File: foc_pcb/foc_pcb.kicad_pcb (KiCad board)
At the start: 2 copper layers, 114.3 x 128.3 mm, 70 parts, among them IC1 AS5600-ASOT, J1 Conn_01x03, J10 Conn_02x03_Top_Bottom, J11 Conn_01x03, J12 10118193-0001LF, J2 Conn_01x03, J3 Conn_01x03, J4 Conn_01x04, J5 XT60PW-M, J6 XT60PW-M, J7 Conn_01x02, J8 Conn_01x02, J9 Conn_01x02, SW1 SW_Push, U1 DRV8313PWPR, U2 ATMEGA328P-AU, U3 BSS138-7-F, U4 BSS138-7-F, U5 CH340C, Y1 ABM3-16MHZ

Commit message: V2 redesign done, needs review
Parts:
- removed D2: 1N5819HW-7-F, 1N5819HW-7-F:SOD3715X145N
- removed D3: LED, KT-0603R:LED0603-RD
- removed H10, H11, H12, H9: boardMount, MountingHole:MountingHole_3.2mm_M3
- removed H5, H6, H7, H8: motorMount, MountingHole:MountingHole_3.2mm_M3
- removed J11, J2: Conn_01x03, Connector_PinHeader_2.54mm:PinHeader_1x03_P2.54mm_Vertical
- removed J4: Conn_01x04, Connector_PinHeader_2.54mm:PinHeader_1x04_P2.54mm_Vertical
- removed J7: Conn_01x02, Connector_PinHeader_2.54mm:PinHeader_1x02_P2.54mm_Vertical
- added U6: ~, XIAO-ESP32S3:MOUDLE14P-SMD-2.54-21X17.8MM, F.Cu at (287.7, 126.4)
- added U7: BSS138-7-F, BSS138-7-F:SOT95P240X110-3N, F.Cu at (285.8, 113.0)
- C1, C10, C12, C16, C17, C2, C3, C4, C6, C7, C8, C9, R1, R10, R12, R13, R14, R15, R16, R17, R18, R2, R3, R5, R6, R7: moved to F.Cu
- C11: value VT1V101M-CRE77 -> UWT1V101MCL1GS; footprint VT1V101M-CRE77:CAP-SMD_BD6.3-L6.6-W6.6-FD -> UWT1V101MCL1GS:PCAP_6.3x7.7-ELECT_NCA-L
- C13, C14, IC1, R11, R9: moved to B.Cu
- D1: value 19-213/Y2C-CQ2R2L/3T(CY) -> 1N5819HW-7-F; footprint simpleFOC_led:LED0603-RD-YELLOW -> 1N5819HW-7-F:SOD3715X145N
- D5: footprint KT-0603R:LED0603-RD -> LED_SMD:LED_0603_1608Metric
- J1: value Conn_01x03 -> MPU6050; footprint Connector_PinHeader_2.54mm:PinHeader_1x03_P2.54mm_Vertical -> Connector_PinHeader_2.54mm:PinHeader_1x08_P2.54mm_Vertical
- R4, R8: value 1k -> 10k; moved to F.Cu
- U2: footprint ATMEGA328P-AU-NEW:QFP80P900X900X120-32N -> ATMEGA328P-AU:QFP80P900X900X120-32N
- moved J12 240.4 mm to (229.4, 100.3), turned to 180 degrees
- moved J1 209.3 mm to (284.5, 104.1), turned to -90 degrees
- moved SW1 203.5 mm to (220.2, 120.7), turned to 0 degrees
- moved R5 201.9 mm to (231.6, 118.1), turned to 0 degrees
- moved C9 200.8 mm to (252.7, 114.3), turned to 180 degrees
- moved U5 199.2 mm to (246.4, 114.3)
- moved C12 197.9 mm to (252.0, 109.2), turned to 180 degrees
- moved R13 197.0 mm to (215.1, 105.4), turned to 0 degrees
- moved R6 193.9 mm to (235.4, 118.1)
- moved C10 193.0 mm to (252.0, 111.8), turned to 0 degrees
- moved C4 191.3 mm to (214.6, 118.1), turned to -90 degrees
- moved R7 191.1 mm to (237.5, 118.1)
- moved R14 190.8 mm to (215.1, 109.2), turned to 0 degrees
- moved VR1 190.3 mm to (218.4, 114.3)
- moved R10 187.9 mm to (210.0, 143.5)
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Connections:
- net /escl renamed /scl
- net /esda renamed /sda
- net /lvRX renamed /esp_mosi
- net /lvTX renamed /esp_miso
- C10 pad 1: Net-(U5-V3) -> Net-(U5-VCC)
- C12 pad 2: Net-(U5-V3) -> Net-(U5-VCC)
- J1 pad 1: /uRX -> +3.3V
- J1 pad 2: /uTX -> GND
- J1 pad 3: GND -> /esp_scl_1
- R15 pad 1: /3vin -> +3.3V
- R16 pad 2: /aRX1 -> /mosi
- R17 pad 1: /3vin -> +3.3V
- R18 pad 2: /aTX1 -> /miso
- R4 pad 1: VCC -> +3.3V
- R4 pad 2: Net-(D1-A) -> /esp_sck
- R8 pad 1: Net-(D3-A) -> +5V
- U2 pad 12: /aRX1 -> unconnected-(U2-PB0-Pad12)
- U2 pad 13: /aTX1 -> unconnected-(U2-PB1-Pad13)
- U2 pad 14: /aRX2 -> GND
- U2 pad 23: unconnected-(U2-PC0-Pad23) -> /gpio_1
- U2 pad 24: unconnected-(U2-PC1-Pad24) -> /gpio_2
- U2 pad 32: /aTX2 -> unconnected-(U2-PD2-Pad32)
- U3 pad 1: /3vin -> +3.3V
- U3 pad 3: /aRX1 -> /mosi
- U4 pad 1: /3vin -> +3.3V
- U4 pad 3: /aTX1 -> /miso
- U5 pad 16: +5V -> Net-(U5-VCC)
- U5 pad 4: Net-(U5-V3) -> +5V
- VR1 pad 2: Net-(VR1-OUTPUT) -> +5V
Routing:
- net +5V: track 326.2 -> 76.7 mm, vias 9 -> 13
- net /rst: track 168.6 -> 74.3 mm, vias 2 -> 3
- net /aRX1: track 93.7 -> 0.00 mm, vias 2 -> 0
- net /aTX1: track 88.7 -> 0.00 mm, vias 2 -> 0
- net /uRX: track 92.1 -> 8.32 mm, vias 3 -> 0
- net /uTX: track 83.9 -> 9.68 mm, vias 3 -> 0
- net +3.3V: track 38.4 -> 103.4 mm, vias 1 -> 2
- net /out1: track 67.4 -> 15.3 mm, vias 2 -> 0
- net Net-(U2-PD7): track 75.5 -> 23.9 mm, vias 3 -> 2
- net /in1: track 64.7 -> 16.6 mm, vias 0 -> 2
- net /esp_sda_1: track 0.00 -> 47.9 mm, vias 0 -> 1
- net /out2: track 61.3 -> 15.1 mm, vias 2 -> 0
- net /3vin: track 46.2 -> 0.00 mm
- net /aTX2: track 43.3 -> 0.00 mm
- net VCC: track 35.5 -> 76.0 mm, vias 5 -> 2
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- added copper zone on In1.Cu, net +5V
- added copper zone on In2.Cu, net GND
- removed copper zone on B.Cu, net GND
- removed copper zone on F.Cu, net VCC
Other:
- board size 114.3 x 128.3 mm -> 90.2 x 48.3 mm
- copper layers 2 -> 4

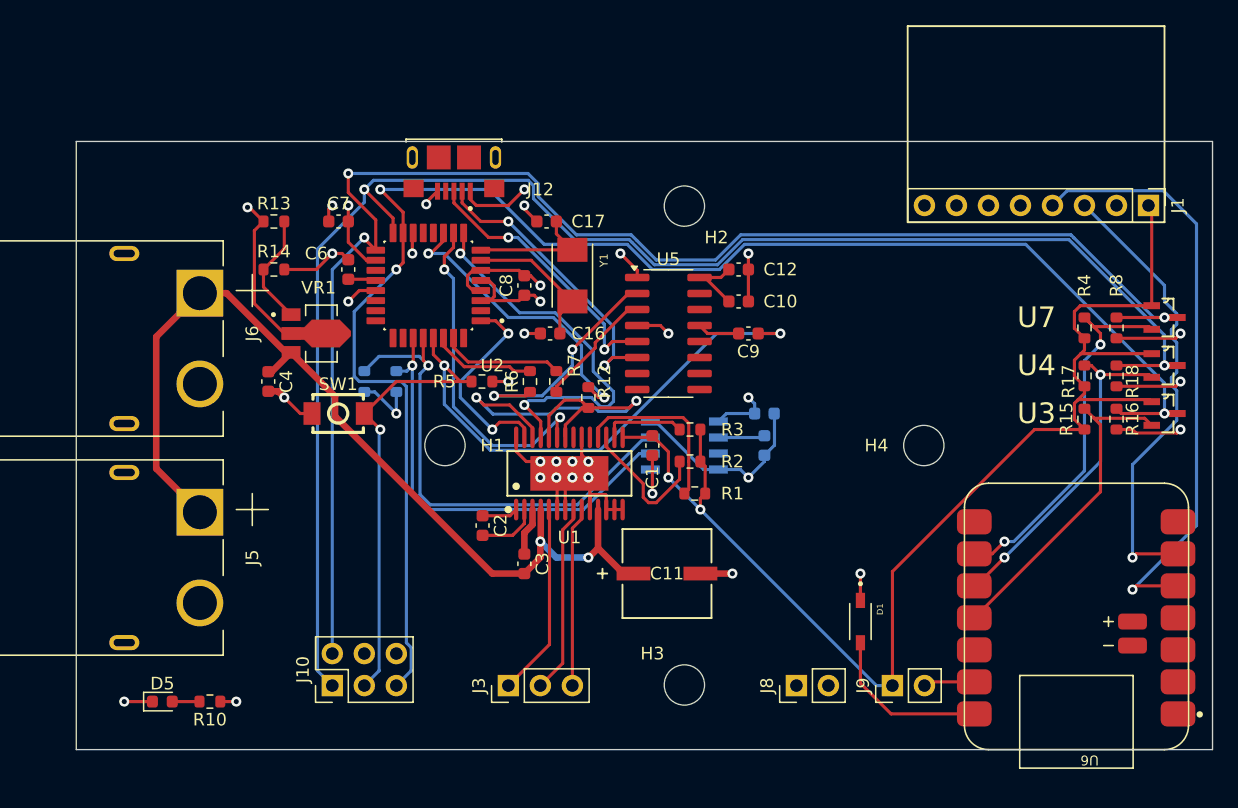
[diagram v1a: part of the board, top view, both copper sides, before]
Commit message: compacted layout, finished V2
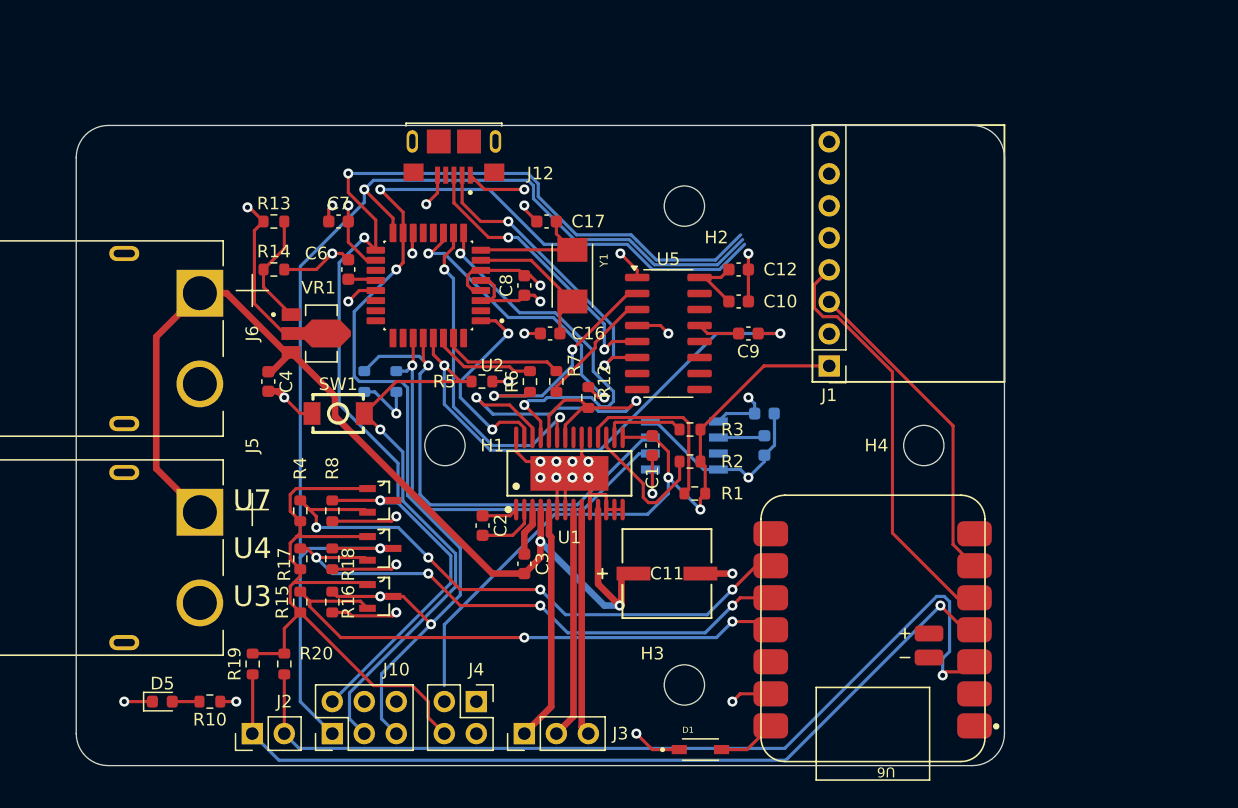
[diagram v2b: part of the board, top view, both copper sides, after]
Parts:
- removed J8, J9: Conn_01x02, Connector_PinHeader_2.54mm:PinHeader_1x02_P2.54mm_Vertical
- added J2: Conn_01x02, Connector_PinHeader_2.54mm:PinHeader_1x02_P2.54mm_Vertical, F.Cu at (213.4, 146.1)
- added J4: power_supply, Connector_PinHeader_2.54mm:PinHeader_2x02_P2.54mm_Vertical, F.Cu at (231.1, 143.5)
- added R19: 10k, Resistor_SMD:R_0603_1608Metric, F.Cu at (213.4, 140.5)
- added R20: 10k, Resistor_SMD:R_0603_1608Metric, F.Cu at (215.9, 140.5)
- moved R15 63.9 mm to (217.2, 135.6)
- moved R16 63.9 mm to (219.7, 135.6)
- moved R17 63.9 mm to (217.2, 132.2)
- moved R18 63.9 mm to (219.7, 132.2)
- moved R4 63.9 mm to (217.2, 128.4)
- moved R8 63.9 mm to (219.7, 128.4)
- moved U3 63.9 mm to (223.5, 135.2)
- moved U4 63.9 mm to (223.5, 131.4)
- moved U7 63.9 mm to (223.5, 127.5)
- moved J1 28.4 mm to (259.1, 116.9), turned to 180 degrees
- moved D1 16.3 mm to (248.9, 147.3), turned to 0 degrees
- moved U6 16.2 mm to (271.5, 127.3)
- moved J3 4.02 mm to (234.9, 146.1)
- moved J10 3.81 mm to (219.7, 146.1)
- moved J12 1.27 mm to (229.4, 99.1)
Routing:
- net /esp_sda_0: track 0.00 -> 72.2 mm, vias 0 -> 1
- net /esp_scl_0: track 0.00 -> 68.8 mm, vias 0 -> 1
- net /mosi: track 124.7 -> 96.3 mm, vias 3 -> 4
- net /miso: track 125.2 -> 97.7 mm
- net /sck: track 120.1 -> 96.3 mm
- net /esp_miso: track 26.7 -> 45.4 mm, vias 2 -> 4
- net /esp_mosi: track 26.1 -> 44.7 mm, vias 0 -> 2
- net /esp_sck: track 30.4 -> 48.9 mm, vias 2 -> 4
- net /esp_sda_1: track 47.9 -> 33.2 mm, vias 1 -> 0
- net /esp_scl_1: track 36.9 -> 25.7 mm, vias 1 -> 0
- net /rst: track 74.3 -> 84.0 mm
- net Net-(U6-5V): track 13.3 -> 4.69 mm
- net VCC: track 76.0 -> 83.3 mm
- net +3.3V: track 103.4 -> 108.3 mm
- net /out3: track 14.3 -> 19.0 mm
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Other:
- board size 90.2 x 48.3 mm -> 73.7 x 50.8 mm

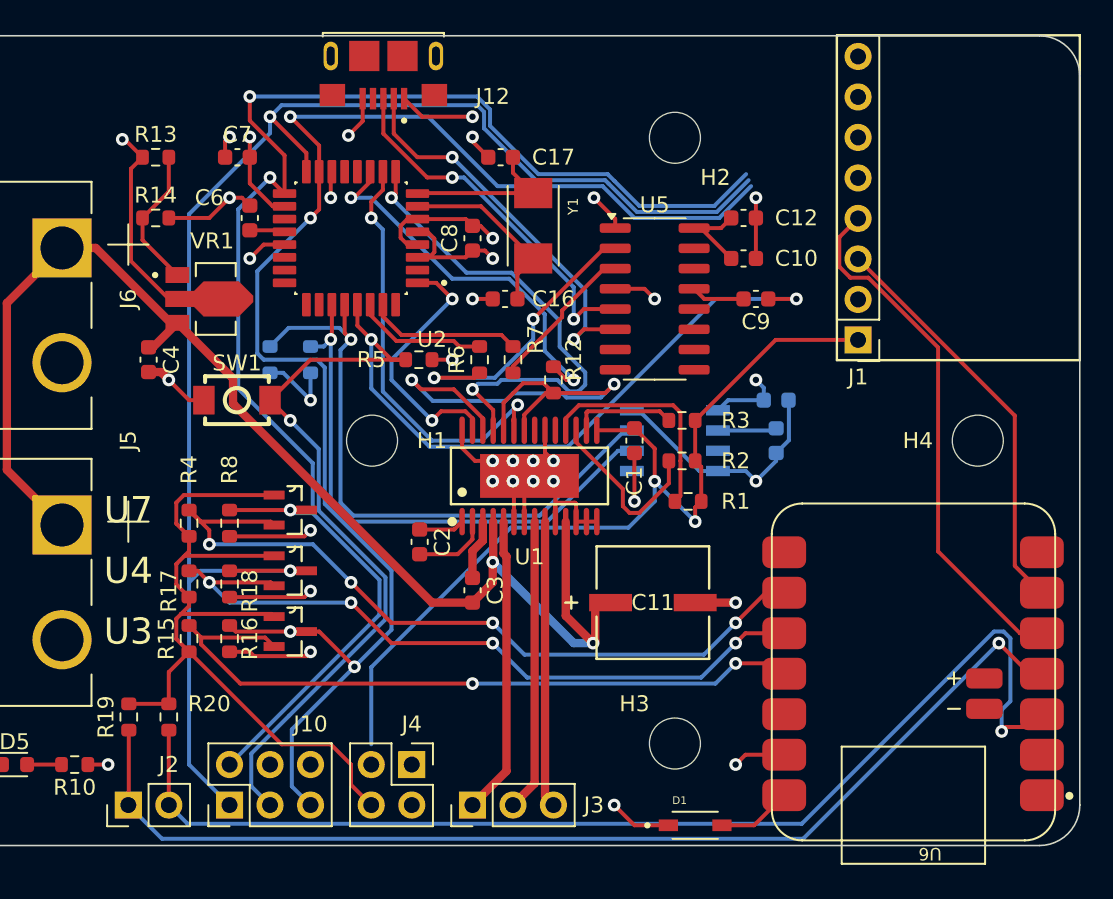
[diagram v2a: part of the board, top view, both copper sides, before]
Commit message: fixed some drc and added silkscreen
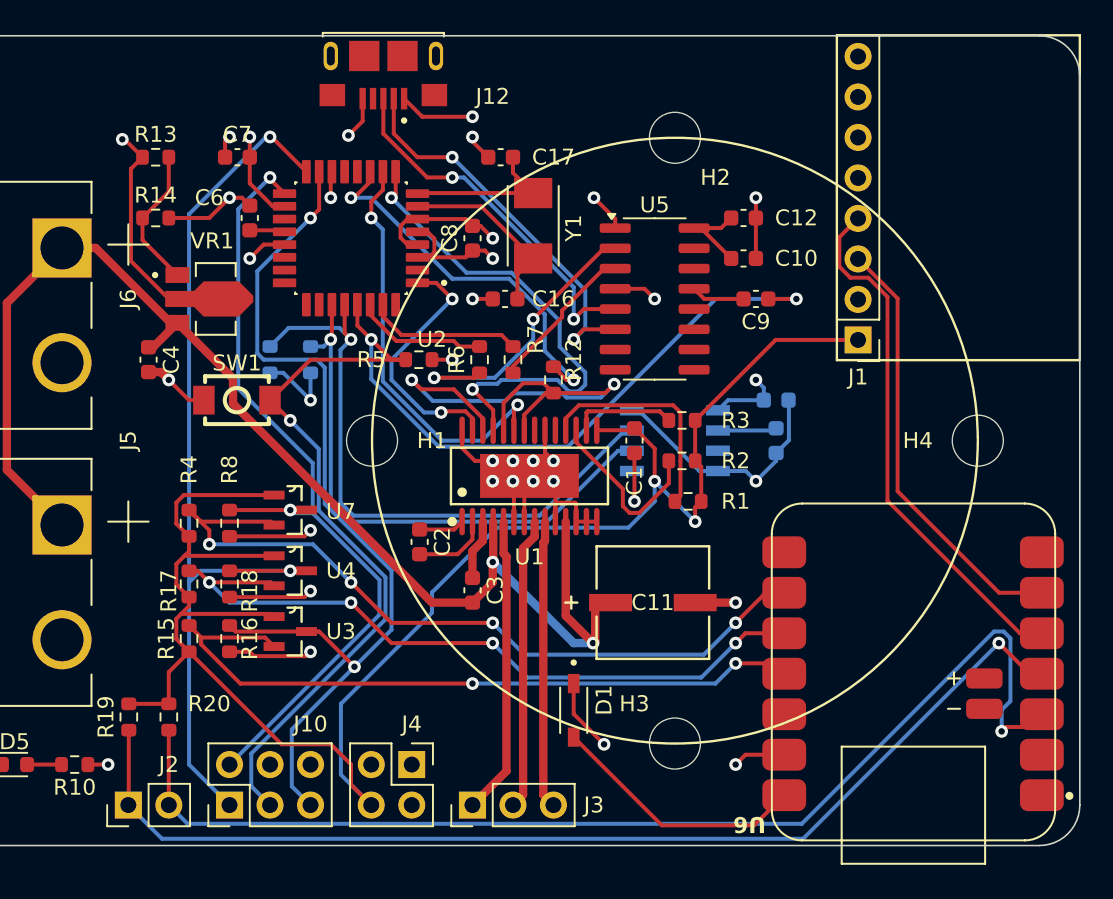
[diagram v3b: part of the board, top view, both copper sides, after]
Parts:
- moved D1 10.5 mm to (241.3, 140.1), turned to -90 degrees
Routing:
- net /sck: track 96.3 -> 53.9 mm, vias 3 -> 2
- net /mosi: track 96.3 -> 58.8 mm, vias 4 -> 2
- net /miso: track 97.7 -> 60.9 mm
- net Net-(U6-5V): track 4.69 -> 16.3 mm
- net +3.3V: track 108.3 -> 114.2 mm
- net /esp_scl_1: track 25.7 -> 27.3 mm
- net +5V: track 77.0 -> 77.7 mm
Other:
- board text added: "AVANINDER.COM"
- board text added: "GimbalFOC"
- board text added: "v2.0"

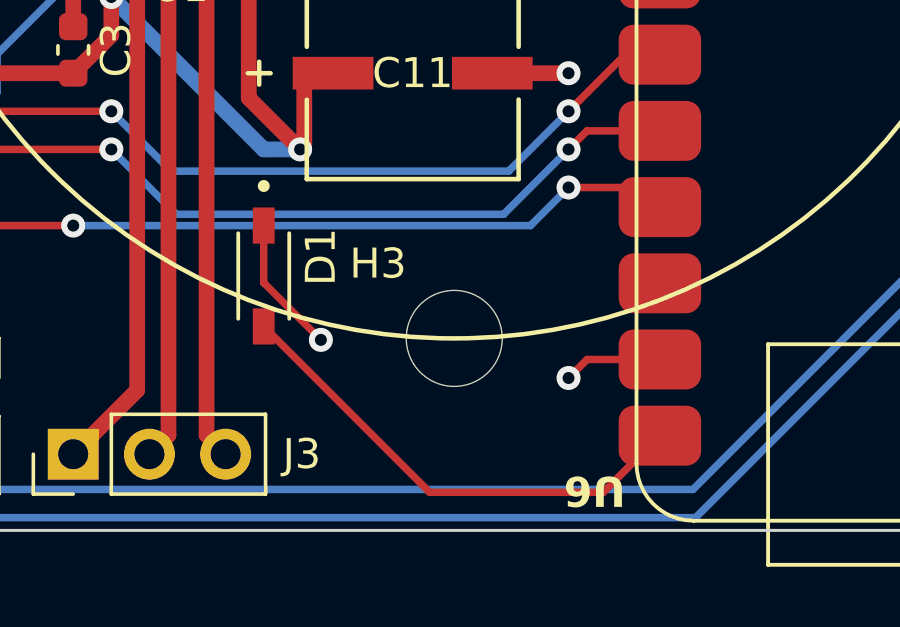
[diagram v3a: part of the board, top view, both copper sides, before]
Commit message: added kicad preview
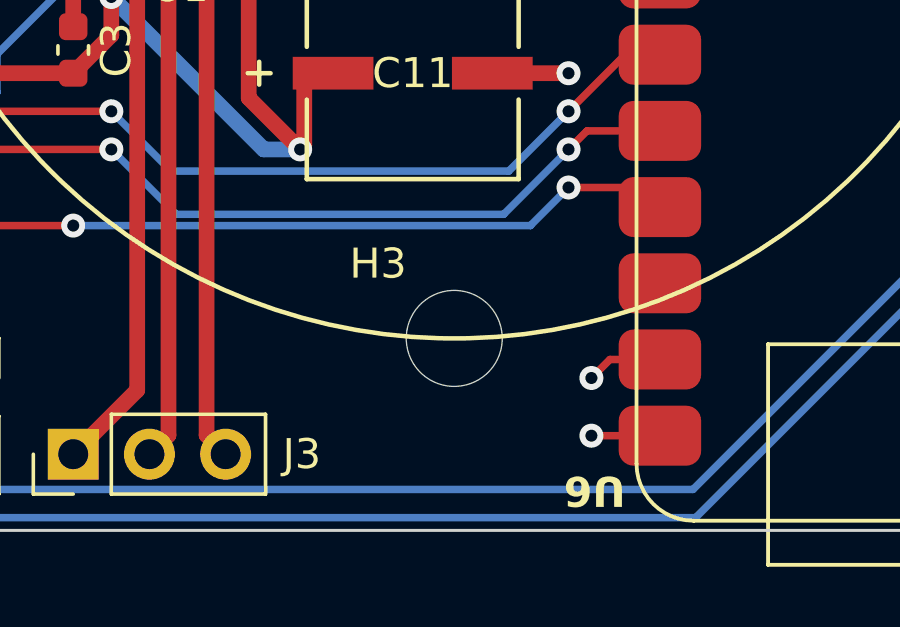
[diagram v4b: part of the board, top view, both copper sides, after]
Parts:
- removed D1: 1N5819HW-7-F, 1N5819HW-7-F:SOD3715X145N
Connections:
- U6 pad 14: Net-(U6-5V) -> +5V
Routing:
- net Net-(U6-5V): track 16.3 -> 0.00 mm
- net +5V: track 77.7 -> 75.4 mm
- net GND: track 81.3 -> 80.5 mm

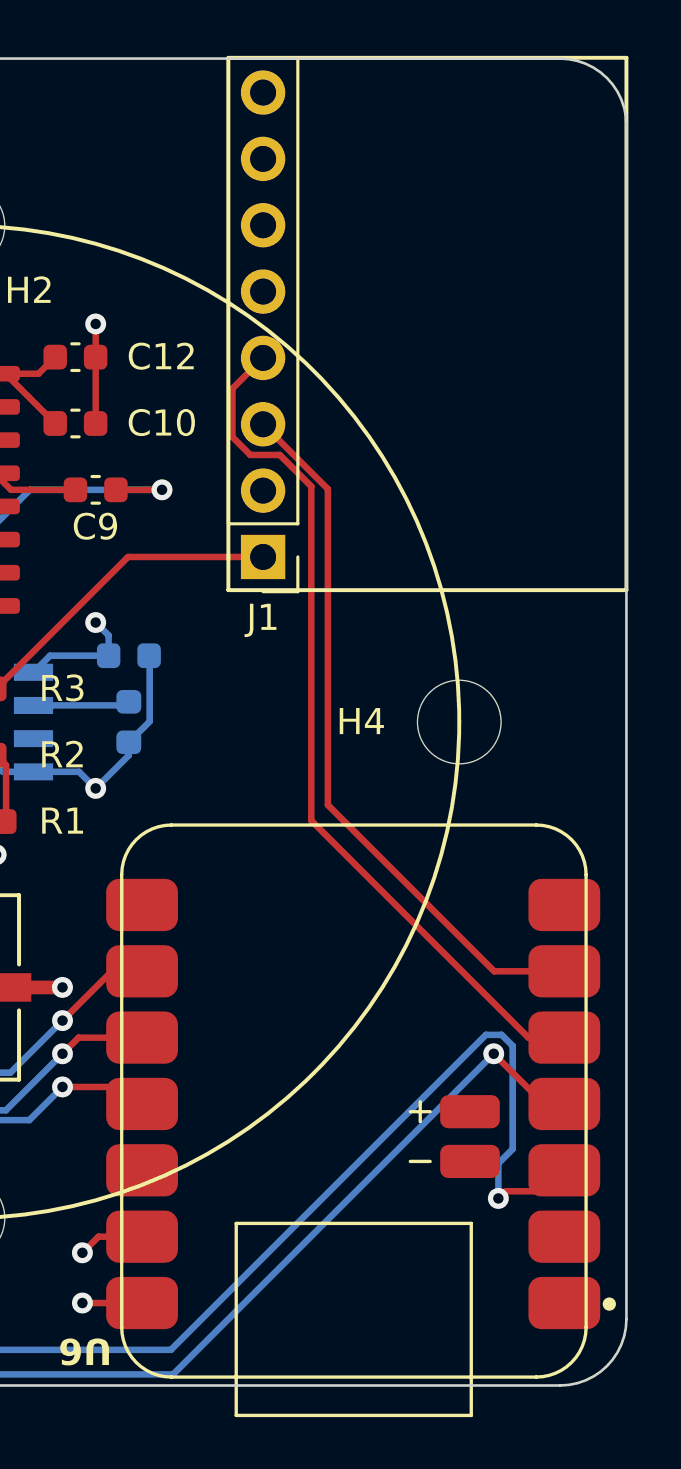
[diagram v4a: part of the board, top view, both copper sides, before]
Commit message: V2 FOC and SPI working
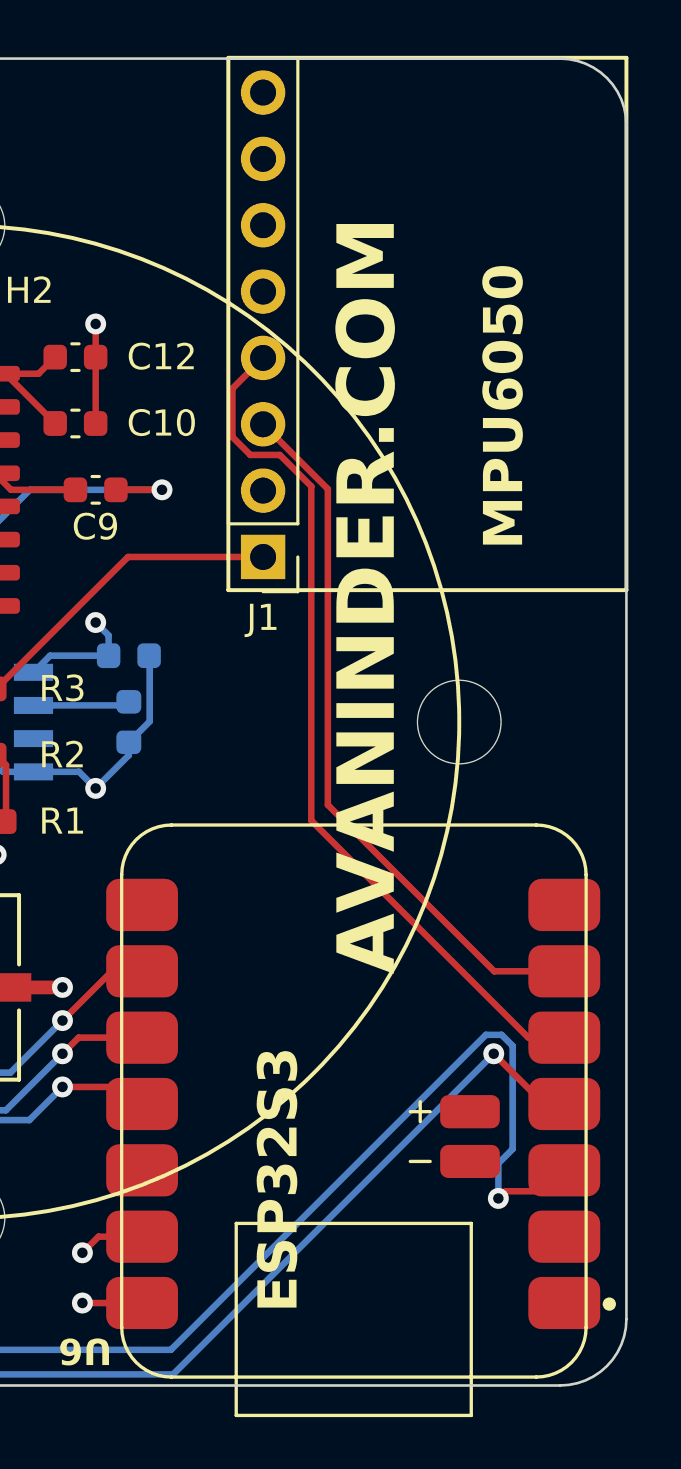
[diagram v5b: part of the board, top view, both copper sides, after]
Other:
- board text added: "ESP32S3"
- board text added: "MPU6050"
